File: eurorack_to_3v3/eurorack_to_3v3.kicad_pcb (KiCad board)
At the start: 2 copper layers, 149 parts, among them J1 header, J2 header, J25 Eurorack Power Header, J3 header, J30 Brain Bus, J4 header, J5 header, J6 header, J7 header, U1 LM324, U10 MOSFET_RK7002BM, U11 MOSFET_RK7002BM, U12 MOSFET_RK7002BM, U13 MOSFET_RK7002BM, U14 74HC165, U15 MCP3208, U17 74HC165, U18 74HC137, U19 BH2227FV, U2 TL074CDT, U20 74HC595, U21 MOSFET_RK7002BM, U22 MOSFET_RK7002BM, U23 MOSFET_RK7002BM, U24 MOSFET_RK7002BM, U3 LM324, U4 MCP6009, U5 MOSFET_RK7002BM, U6 MOSFET_RK7002BM, U7 MOSFET_RK7002BM, U8 MOSFET_RK7002BM, U9 MCP6009

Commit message: continuing Big One Little One PCB layout
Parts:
- added H1: MountingHole, MountingHole:MountingHole_3.5mm, F.Cu at (116.4, 43.4)
- added H2: MountingHole, MountingHole:MountingHole_3.5mm, F.Cu at (146.9, 82.0)
- added H3: MountingHole, MountingHole:MountingHole_3.5mm, F.Cu at (99.3, 49.1)
- added H4: MountingHole, MountingHole:MountingHole_3.5mm, F.Cu at (99.3, 57.6)
- J1: value header -> cv_in_2; moved to B.Cu
- J2: value header -> gate_in_2
- J25: moved to B.Cu
- J3: value header -> gate_in_1
- J4: value header -> cv_in_1
- J5: value header -> gate_in_3
- J6: value header -> gate_out; moved to B.Cu
- J7: value header -> cv_out; moved to B.Cu
- moved C5 111.5 mm to (65.6, 94.9)
- moved C1 111.5 mm to (62.7, 95.0)
- moved C15 111.5 mm to (20.7, 116.7)
- moved C16 111.5 mm to (16.2, 116.7)
- moved C18 111.5 mm to (41.7, 97.3)
- moved C19 111.5 mm to (33.7, 106.1)
- moved C22 111.5 mm to (41.7, 99.3)
- moved C23 111.5 mm to (27.9, 112.7)
- moved C3 111.5 mm to (65.1, 92.9)
- moved D1 111.5 mm to (10.8, 116.8)
- moved D2 111.5 mm to (4.49, 116.8)
- moved R1 111.5 mm to (-11.2, 133.4)
- moved R10 111.5 mm to (-0.07, 130.4)
- moved R11 111.5 mm to (-4.33, 127.1)
- moved R12 111.5 mm to (-4.33, 123.8)
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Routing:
- net GNDD: track 0.00 -> 112.5 mm, vias 0 -> 2
- net +3V3: track 0.00 -> 79.7 mm, vias 0 -> 2
- net Net-(R77-Pad1): track 0.00 -> 37.3 mm
- net Net-(C12-Pad2): track 0.00 -> 35.8 mm
- net Net-(C9-Pad2): track 0.00 -> 34.5 mm
- net Net-(R63-Pad1): track 0.00 -> 34.4 mm
- net Net-(C10-Pad2): track 0.00 -> 32.4 mm
- net /cv_to_3v3_B/cv_in_1: track 0.00 -> 31.1 mm, vias 0 -> 1
- net /cv_to_3v3_B/cv_in_2: track 0.00 -> 30.5 mm, vias 0 -> 1
- net Net-(R83-Pad1): track 0.00 -> 29.1 mm
- net Net-(R39-Pad1): track 0.00 -> 28.3 mm
- net /cv_to_3v3_B/cv_in_4: track 0.00 -> 27.7 mm, vias 0 -> 1
- net /cv_to_3v3_B/cv_in_3: track 0.00 -> 27.4 mm, vias 0 -> 1
- net Net-(R69-Pad1): track 0.00 -> 27.0 mm
- net GND: track 0.00 -> 26.6 mm
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- added copper zone on B.Cu, net GNDD
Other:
- board outline added: 47.5 x 106.5 mm
- board text added: "3U, 14HP"
- board text added: "TODO: 3.05mm diameter holes for 6-32 screws"

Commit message: finished input stages PCB layout
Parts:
- J30: moved to B.Cu
- moved U14 157.1 mm to (144.5, 92.9)
- moved U17 141.0 mm to (153.6, 92.9)
- moved U15 136.4 mm to (132.4, 95.0), turned to 270 degrees
- moved U20 126.3 mm to (145.2, 113.1), turned to 90 degrees
- moved U18 124.3 mm to (152.1, 103.8), turned to 90 degrees
- moved U19 107.6 mm to (143.0, 103.9)
- moved J30 14.3 mm to (141.9, 126.7), turned to 270 degrees
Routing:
- net +3V3: track 79.7 -> 255.4 mm, vias 2 -> 13
- net /SCK: track 0.00 -> 80.4 mm, vias 0 -> 4
- net /LOAD_GATES: track 0.00 -> 77.0 mm, vias 0 -> 4
- net /gate_to_3v3_A/GATE_3V3_4: track 1.29 -> 73.8 mm, vias 0 -> 4
- net /POCI: track 0.00 -> 72.2 mm, vias 0 -> 3
- net /gate_to_3v3_A/GATE_3V3_3: track 1.29 -> 67.4 mm, vias 0 -> 4
- net /PICO: track 0.00 -> 63.3 mm, vias 0 -> 2
- net GND: track 26.6 -> 88.5 mm, vias 0 -> 4
- net /gate_to_3v3_A/GATE_3V3_2: track 1.29 -> 62.0 mm, vias 0 -> 4
- net /AREF_-10V: track 13.6 -> 72.6 mm, vias 2 -> 6
- net /gate_to_3v3_B/GATE_3V3_4: track 1.19 -> 59.9 mm, vias 0 -> 2
- net /gate_to_3v3_A/GATE_3V3_1: track 1.19 -> 58.9 mm, vias 0 -> 2
- net /gate_to_3v3_B/GATE_3V3_1: track 1.29 -> 57.0 mm, vias 0 -> 4
- net /gate_to_3v3_C/GATE_3V3_4: track 1.39 -> 56.9 mm, vias 0 -> 4
- net /gate_to_3v3_B/GATE_3V3_2: track 1.29 -> 54.8 mm, vias 0 -> 4
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
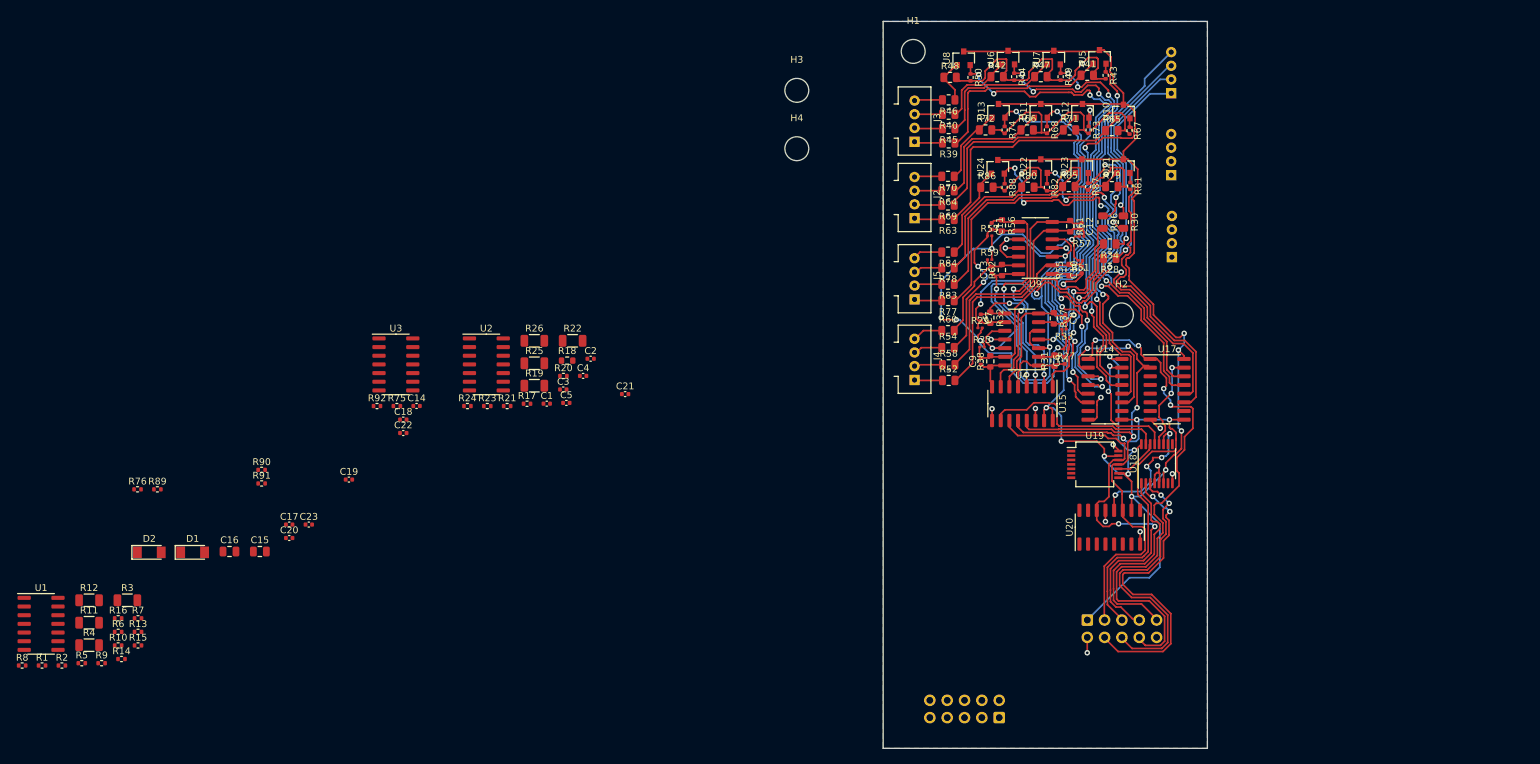
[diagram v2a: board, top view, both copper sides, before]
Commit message: finished pcb layout, just a few bugs from rules checker
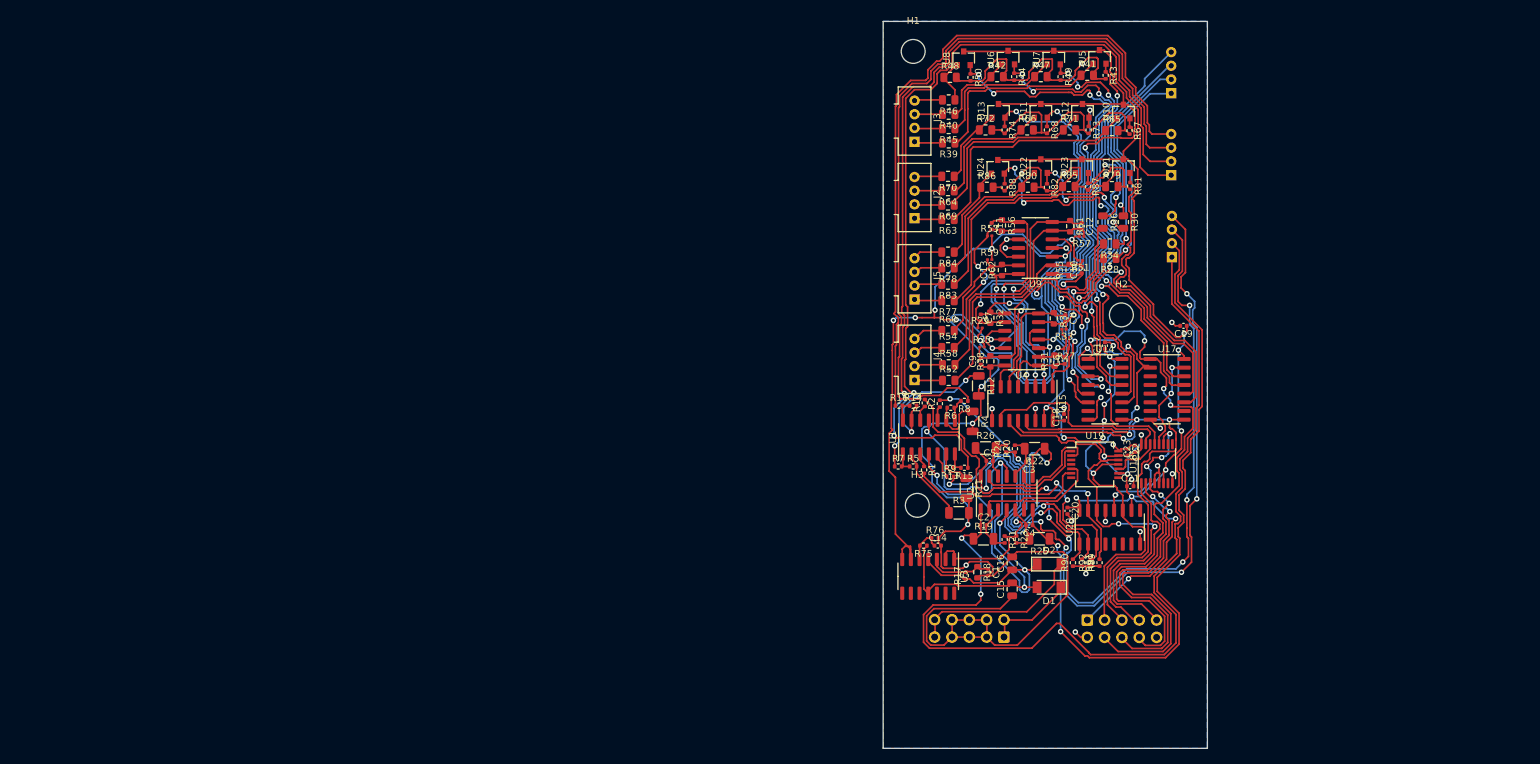
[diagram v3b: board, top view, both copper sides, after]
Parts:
- removed H4: MountingHole, MountingHole:MountingHole_3.5mm
- moved R8 143.4 mm to (123.9, 94.6), turned to 180 degrees
- moved R89 138.4 mm to (143.7, 118.3), turned to 90 degrees
- moved R2 134.2 mm to (120.3, 95.0), turned to 90 degrees
- moved R12 134.1 mm to (126.0, 92.4), turned to 270 degrees
- moved R4 133.5 mm to (125.1, 97.6), turned to 270 degrees
- moved U1 132.9 mm to (118.7, 99.9), turned to 90 degrees
- moved R1 132.4 mm to (118.0, 104.7), turned to 270 degrees
- moved D2 131.8 mm to (136.3, 118.5)
- moved R11 130.0 mm to (124.2, 107.4), turned to 270 degrees
- moved R9 127.3 mm to (121.8, 105.7)
- moved R6 126.3 mm to (121.9, 95.6), turned to 180 degrees
- moved D1 125.6 mm to (136.3, 121.9), turned to 180 degrees
- moved R5 125.2 mm to (116.4, 104.2)
- moved C19 124.3 mm to (156.0, 83.6), turned to 180 degrees
- moved R15 123.8 mm to (123.9, 104.4), turned to 180 degrees
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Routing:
- net GND: track 88.5 -> 241.1 mm, vias 4 -> 8
- net /3v3_to_cv/CV_OUT_1: track 0.00 -> 135.4 mm, vias 0 -> 2
- net /3v3_to_gate/gate_out_2: track 0.00 -> 123.9 mm, vias 0 -> 2
- net /3v3_to_cv/CV_OUT_4: track 0.00 -> 119.4 mm, vias 0 -> 6
- net /3v3_to_gate/gate_out_1: track 0.00 -> 115.5 mm, vias 0 -> 2
- net /3v3_to_gate/gate_out_3: track 0.00 -> 113.9 mm
- net /3v3_to_cv/CV_OUT_3: track 0.00 -> 107.2 mm, vias 0 -> 6
- net /3v3_to_cv/CV_OUT_2: track 0.00 -> 106.0 mm, vias 0 -> 2
- net /3v3_to_gate/gate_out_4: track 0.00 -> 102.1 mm
- net -12V: track 0.00 -> 70.4 mm, vias 0 -> 3
- net +12V: track 0.00 -> 61.4 mm, vias 0 -> 3
- net /AREF_-10V: track 72.6 -> 121.7 mm, vias 6 -> 8
- net /3v3_to_gate/gate_4: track 0.00 -> 46.9 mm, vias 0 -> 2
- net /3v3_to_gate/gate_3: track 0.00 -> 45.5 mm, vias 0 -> 2
- net /3v3_to_gate/gate_2: track 0.00 -> 42.3 mm, vias 0 -> 2
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
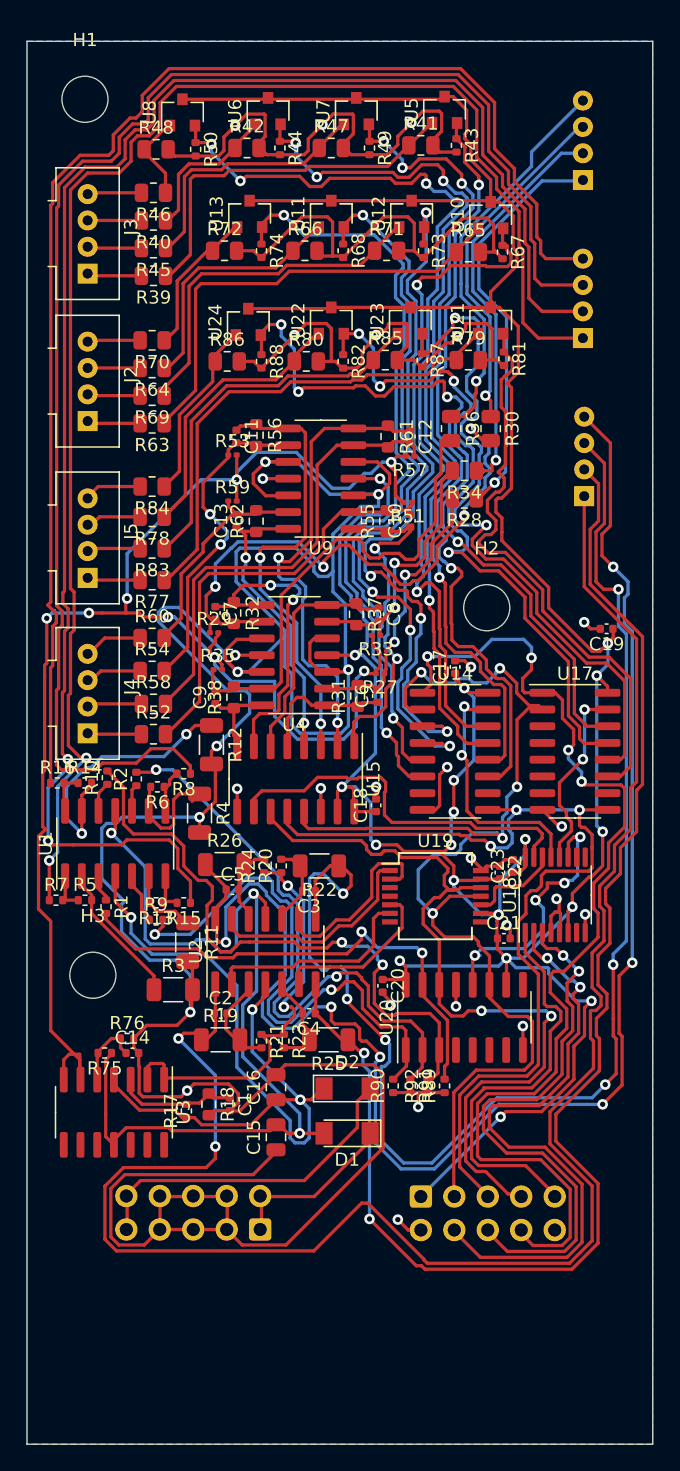
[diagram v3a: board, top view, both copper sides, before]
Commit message: fixed clearance issues with pcb
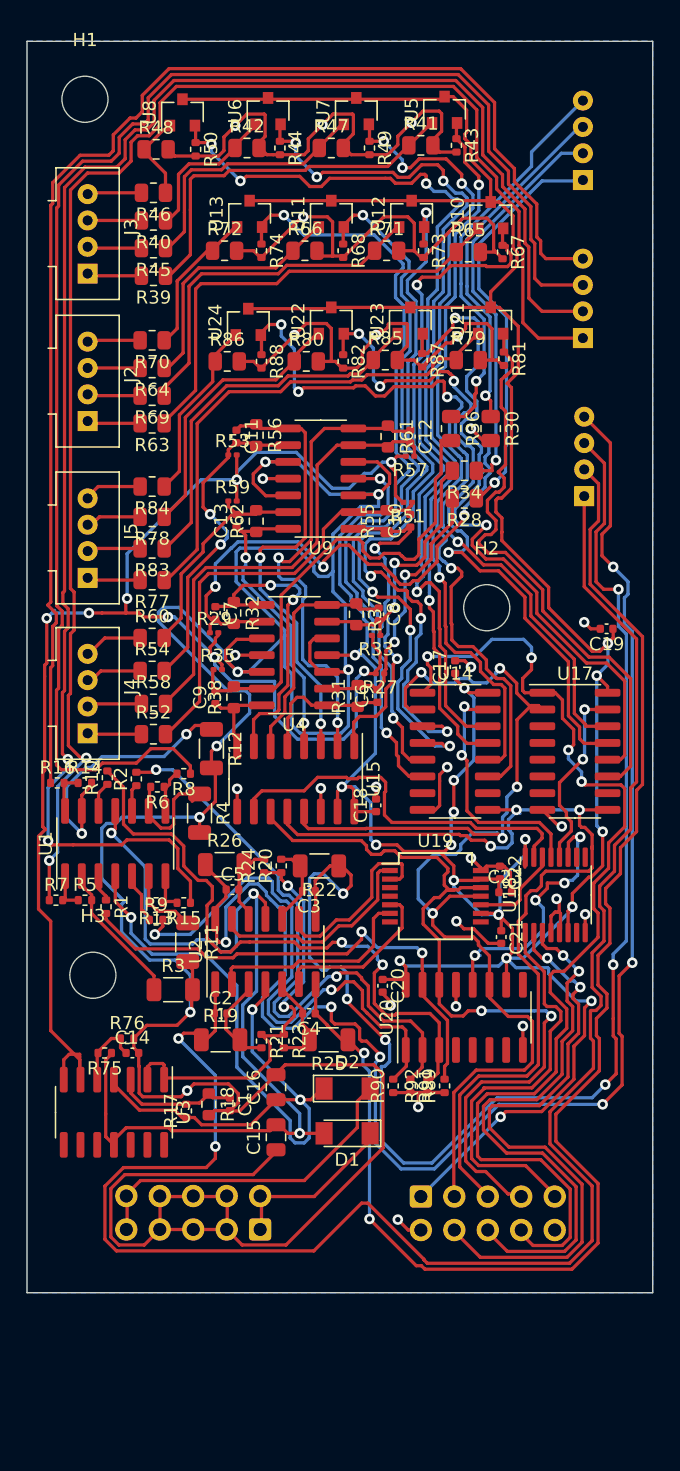
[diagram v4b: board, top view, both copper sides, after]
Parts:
- moved C23 2.09 mm to (148.3, 103.6), turned to 0 degrees
- moved R12 0.30 mm to (126.0, 92.7)
- moved C21 0.22 mm to (148.0, 107.0), turned to 270 degrees
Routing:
- net GNDD: track 150.0 -> 154.2 mm, vias 24 -> 25
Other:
- board size 47.5 x 106.5 mm -> 47.5 x 95 mm

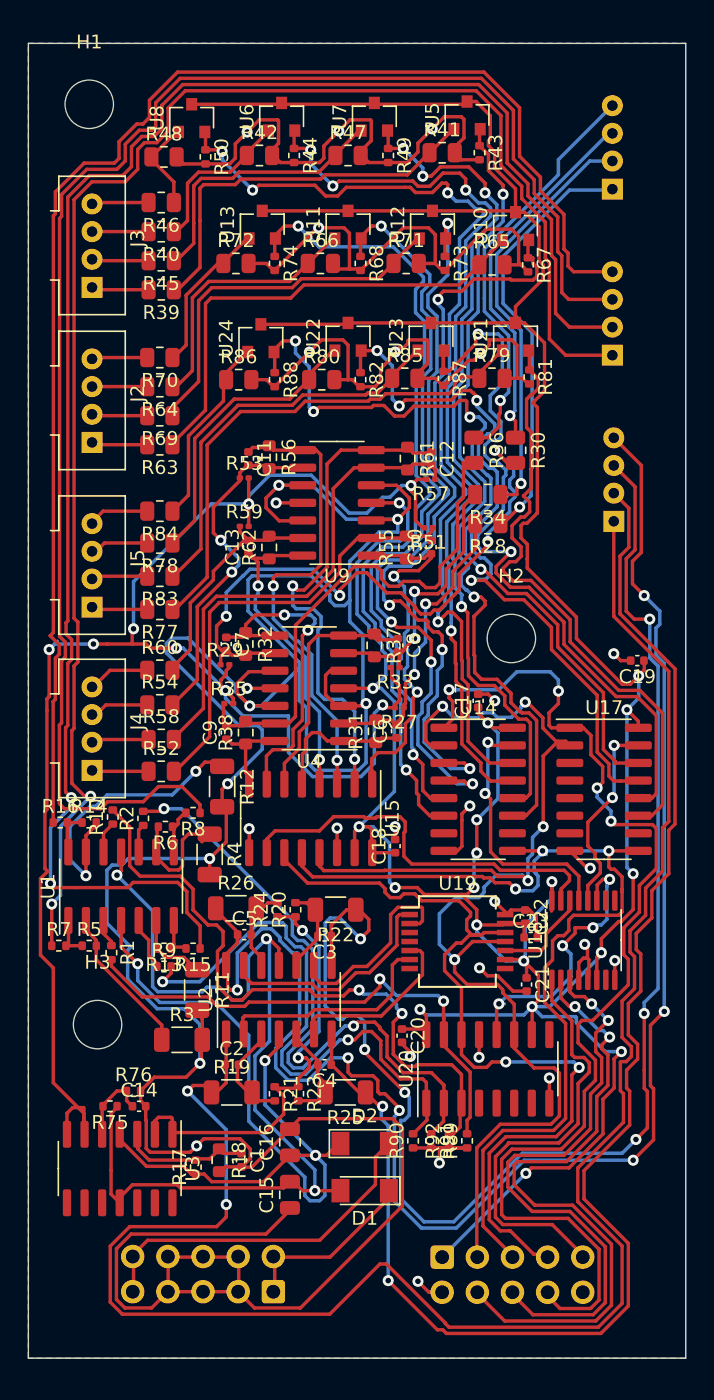
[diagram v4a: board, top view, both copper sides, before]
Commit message: finished pcb, time to order
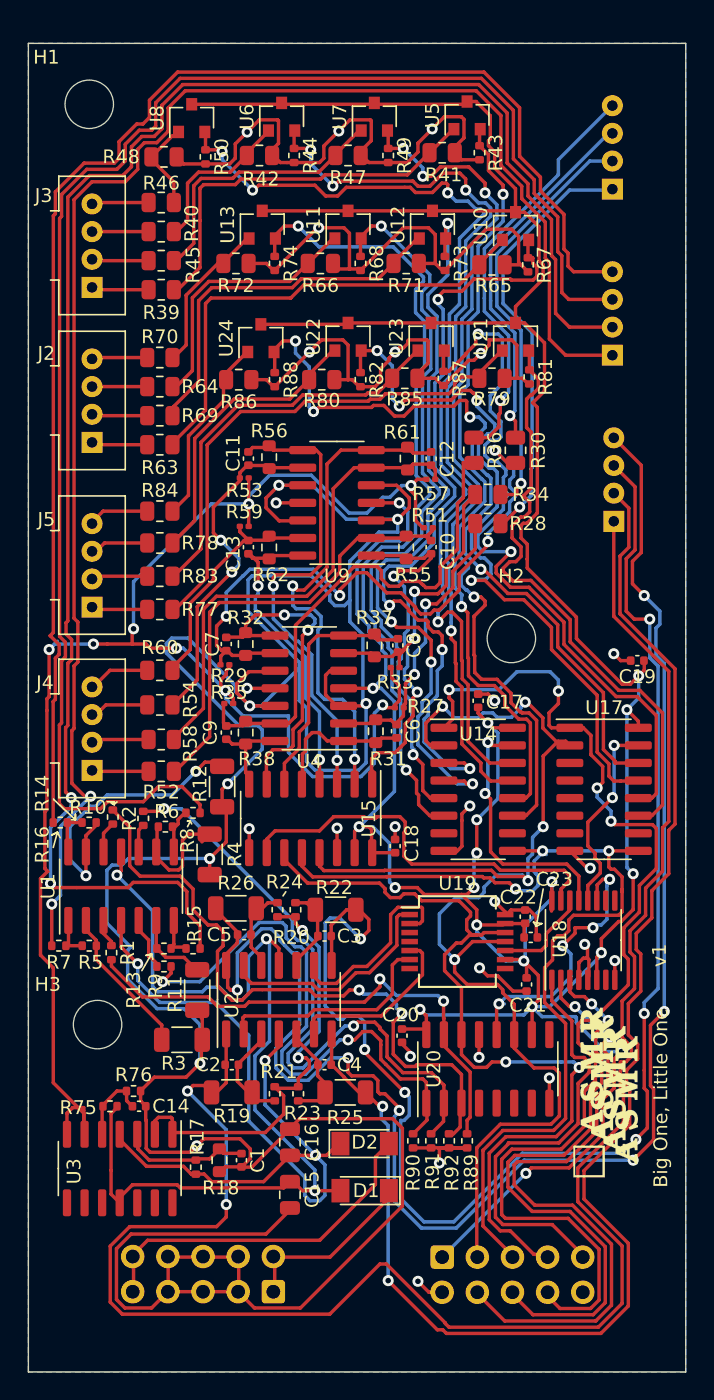
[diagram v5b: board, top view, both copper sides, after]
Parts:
- added G***: LOGO, ASMR_footprints:Silkscreen_mesh, B.Cu at (133.3, 99.8)
- added G***: LOGO, ASMR_footprints:SilkScreen_asmrrrrrrrrr, F.Cu at (154.0, 114.8)
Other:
- board size 47.5 x 95 mm -> 47.5 x 96 mm
- board text added: "Big One, Little One"
- board text added: "BiiiiiiiiG OnE......."
- board text added: "little one"
- board text added: "v1"

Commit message: save in newer kicad format, and begin soldering
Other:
- net class Default removed
